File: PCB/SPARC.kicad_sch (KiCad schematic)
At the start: 86 parts, among them J1 Conn_Coaxial_Power, J2 Conn_Coaxial_Power, J3 Conn_01x06_Female, J4 Conn_01x03_Female, J5 Conn_01x03_Female, J6 Conn_01x06_Female, U1 HV2621, U2 HV2621

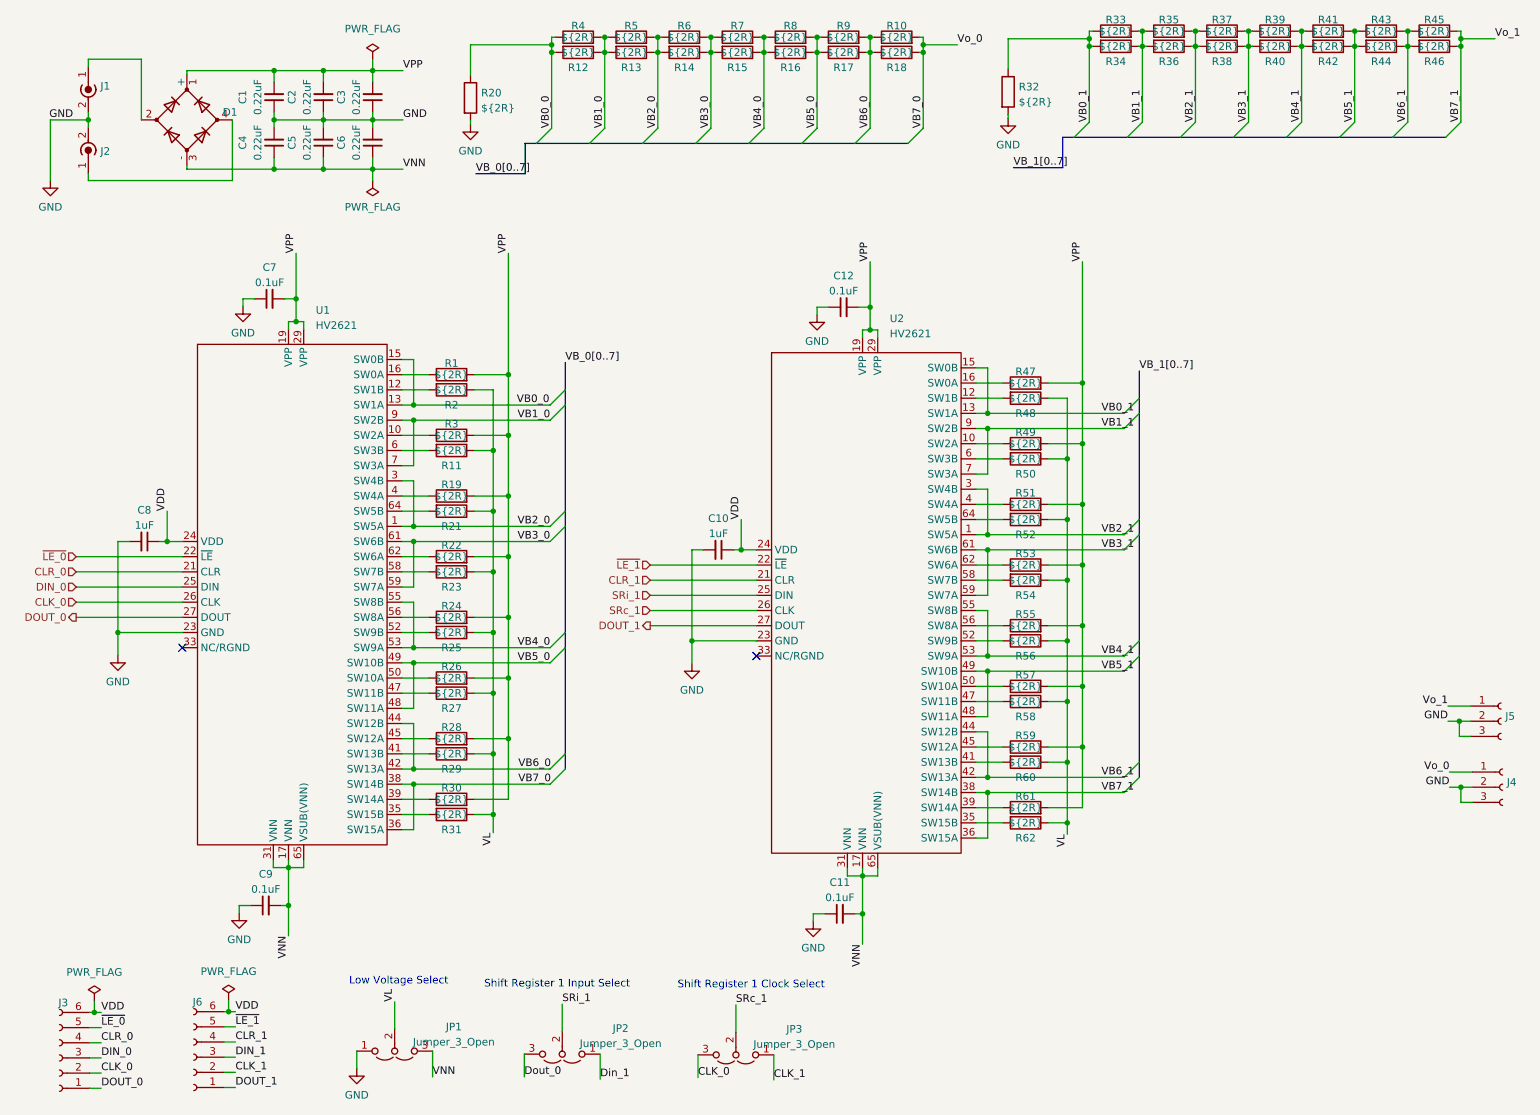
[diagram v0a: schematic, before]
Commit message: Worked on adding second channel
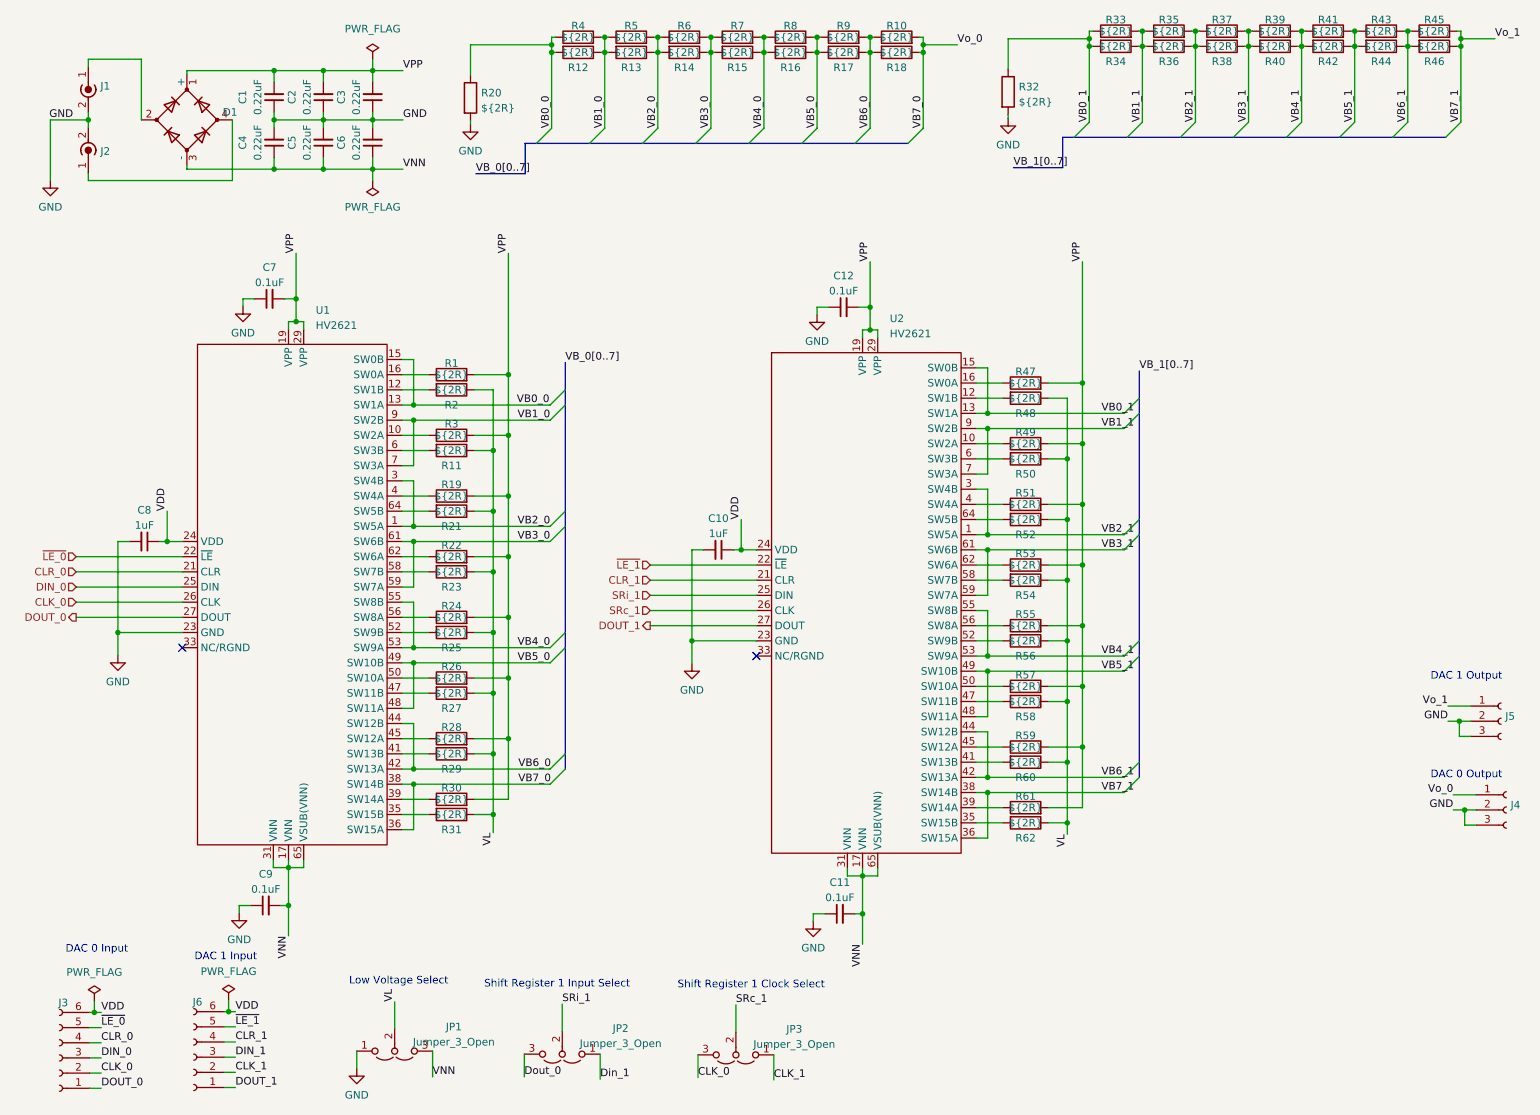
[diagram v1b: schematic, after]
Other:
- note added: "DAC 0 Input"
- note added: "DAC 0 Output"
- note added: "DAC 1 Input"
- note added: "DAC 1 Output"
- moved on the sheet: J4
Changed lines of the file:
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@@
   (junction (at 97.028 88.392) (diameter 0) (color 0 0 0 0)
   )
-  (junction (at 256.54 147.32) (diameter 0) (color 0 0 0 0)
+  (junction (at 257.175 151.13) (diameter 0) (color 0 0 0 0)
   )
   (junction (at 127.762 122.809) (diameter 0) (color 0 0 0 0)
@@
     (stroke (width 0) (type default) (color 0 0 0 0))
   )
-  (wire (pts (xy 254.635 147.32) (xy 256.54 147.32))
+  (wire (pts (xy 255.27 151.13) (xy 257.175 151.13))
     (stroke (width 0) (type default) (color 0 0 0 0))
   )
@@
     (stroke (width 0) (type default) (color 0 0 0 0))
   )
-  (wire (pts (xy 254.635 144.78) (xy 258.445 144.78))
+  (wire (pts (xy 255.27 148.59) (xy 259.08 148.59))
     (stroke (width 0) (type default) (color 0 0 0 0))
   )
@@
     (stroke (width 0) (type default) (color 0 0 0 0))
   )
-  (wire (pts (xy 256.54 147.32) (xy 256.54 149.86))
+  (wire (pts (xy 257.175 151.13) (xy 257.175 153.67))
     (stroke (width 0) (type default) (color 0 0 0 0))
   )
@@
     (stroke (width 0) (type default) (color 0 0 0 0))
   )
-  (wire (pts (xy 256.54 147.32) (xy 258.445 147.32))
+  (wire (pts (xy 257.175 151.13) (xy 259.08 151.13))
     (stroke (width 0) (type default) (color 0 0 0 0))
   )
@@
     (stroke (width 0) (type default) (color 0 0 0 0))
   )
-  (wire (pts (xy 256.54 149.86) (xy 258.445 149.86))
+  (wire (pts (xy 257.175 153.67) (xy 259.08 153.67))
     (stroke (width 0) (type default) (color 0 0 0 0))
   )
@@
     (stroke (width 0) (type default) (color 0 0 0 0))
   )
+  (text "DAC 1 Output" (at 251.46 129.54 0)
+    (effects (font (size 1.27 1.27)) (justify left bottom))
+  )
   (text "Low Voltage Select" (at 70.358 180.594 0)
+    (effects (font (size 1.27 1.27)) (justify left bottom))
+  )
+  (text "DAC 0 Output" (at 251.46 146.05 0)
+    (effects (font (size 1.27 1.27)) (justify left bottom))
+  )
+  (text "DAC 1 Input" (at 44.45 176.53 0)
+    (effects (font (size 1.27 1.27)) (justify left bottom))
+  )
+  (text "DAC 0 Input" (at 22.86 175.26 0)
     (effects (font (size 1.27 1.27)) (justify left bottom))
   )
@@
     (effects (font (size 1.27 1.27)) (justify left bottom))
   )
-  (label "Vo_0" (at 254.635 144.78 180)
+  (label "Vo_0" (at 255.27 148.59 180)
     (effects (font (size 1.27 1.27)) (justify right bottom))
   )
@@
     (effects (font (size 1.27 1.27)) (justify left bottom))
   )
-  (label "GND" (at 254.635 147.32 180)
+  (label "GND" (at 255.27 151.13 180)
     (effects (font (size 1.27 1.27)) (justify right bottom))
   )
@@
     (pin "2")
   )
-  (symbol (lib_id "Connector:Conn_01x03_Female") (at 263.525 147.32 0) (unit 1)
+  (symbol (lib_id "Connector:Conn_01x03_Female") (at 264.16 151.13 0) (unit 1)
     (in_bom yes) (on_board yes) (fields_autoplaced)
-    (property "Reference" "J4" (id 0) (at 264.2362 146.4853 0)
+    (property "Reference" "J4" (id 0) (at 264.8712 150.2953 0)
       (effects (font (size 1.27 1.27)) (justify left))
     )
-    (property "Value" "Conn_01x03_Female" (id 1) (at 264.2362 149.0222 0)
+    (property "Value" "Conn_01x03_Female" (id 1) (at 264.8712 152.8322 0)
       (effects (font (size 1.27 1.27)) (justify left) hide)
     )
-    (property "Footprint" "Connector_PinHeader_2.54mm:PinHeader_1x03_P2.54mm_Vertical" (id 2) (at 263.525 147.32 0)
-      (effects (font (size 1.27 1.27)) hide)
-    )
-    (property "Datasheet" "~" (id 3) (at 263.525 147.32 0)
-      (effects (font (size 1.27 1.27)) hide)
-    )
+    (property "Footprint" "Connector_PinHeader_2.54mm:PinHeader_1x03_P2.54mm_Vertical" (id 2) (at 264.16 151.13 0)
+      (effects (font (size 1.27 1.27)) hide)
+    )
+    (property "Datasheet" "~" (id 3) (at 264.16 151.13 0)
+      (effects (font (size 1.27 1.27)) hide)
+    )
